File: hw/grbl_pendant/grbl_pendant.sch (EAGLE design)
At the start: 7 parts, among them IC1 ATMEGA644A, IC2 FT232RL, IC3 FT232RL, X1 PN61729-S, X2 PN61729-S

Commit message: sch/brd files updated
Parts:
- removed IC1: ATMEGA644A, atmel:ATMEGA644A
- removed IC3: FT232RL, ftdichip:FT232RL
- added C10: 100n, rcl:C-EUC0805
- added C2, C4: 20p, rcl:C-EUC0603K
- added C5, C6, C7: 100n, rcl:C-EUC0603K
- added C8, C9: 10u, rcl:C-EUC0805
- added CON1: MOLEX-53261-0671, SchlegelAr_Master:MOLEX-53261-0671
- added FERRIT1, FERRIT2, FERRIT3: (no value), rcl:R-EU_M0805
- added JP1: (no value), pinhead-2:PINHD-2X08_2.54
- added JP2: (no value), pinhead-2:PINHD-2X03_2.54
- added Q1: 14.7456 MHz, crystal:CRYSTALHC49UP
- added R1, R2, R3, R7: 220R, rcl:R-EU_R0603
- added R4, R5, R6: 100R, rcl:R-EU_R0603
- added U$1: MEGA162MA*A*, avr-7:MEGA162MA*A*
- added U$2: ARDUINONANO, rocketfarm:ARDUINONANO
- added X3: (no value), con-subd:F25HPS
- C1: value 100n -> 10u; device rcl:C-EUC0603 -> rcl:C-EUC0805
- X2: value PN61729-S -> (none); device con-berg:PN61729-S -> con-subd:F25HPS
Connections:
- removed net N$1: C1.2, IC3.3V3OUT, IC3.VCCIO
- removed net N$2: IC1.(PCINT24/RXD0)PD0
- removed net N$3: IC1.(PCINT25/TXD0)PD1
- removed net RXD_UC: IC3.RXD
- removed net TXD_UC: IC3.TXD
- removed net USBDM1: IC3.USBDM, X2.2
- removed net USBDP1: IC3.USBDP, X2.3
- new net !RESET: CON1.RESET
- new net BTN1: U$1.(AD0)PA0, X3-19.F
- new net BTN2: U$1.(AD1)PA1, X3-18.F
- new net BTN3: U$1.(AD2)PA2, X3-17.F
- new net BTN4: U$1.(AD3)PA3, X3-16.F
- new net BTN5: U$1.(AD4)PA4, X3-15.F
- new net BTN6: U$1.(AD5)PA5, X3-14.F
- new net BTN_JOG: U$1.(AD6)PA6, X3-13.F
- new net COOLING_ENABLE: U$2.A3, X2-17.F
- new net CYCLE_START/RESUME: U$2.A2, X2-18.F
- new net DISP_D0: U$1.(A8)PC0, X3-3.F
- new net DISP_D1: U$1.(A9)PC1, X3-4.F
- new net DISP_D2: U$1.(A10)PC2, X3-5.F
- new net DISP_D3: U$1.(A11)PC3, X3-6.F
- new net DISP_D4: U$1.(A12)PC4, X3-7.F
- new net DISP_D5: U$1.(A13)PC5, X3-8.F
- new net DISP_D6: U$1.(A14)PC6, X3-9.F
- new net DISP_D7: U$1.(A15)PC7, X3-10.F
- new net DISP_ENABLE: U$1.(ALE)PE1, X3-12.F
- new net DISP_RS: U$1.(OC1B)PE2, X3-11.F
- new net ENCODER_A: U$1.(INT0)PD2, X3-20.F
- new net ENCODER_B: U$1.(INT1)PD3, X3-21.F
- new net ENCODER_BTN: U$1.(INT2)PE0, X3-22.F
- new net FEED/HOLD: U$2.A1, X2-19.F
- new net LED_SHIFT_RCK: U$1.(TOSC2)PD5, X3-23.F, X3-24.F
- new net LED_SHIFT_SCK: U$1.(WR)PD6
- new net LED_SHIFT_SI: U$1.(TOSC1)PD4, X3-25.F
- new net LIMIT_INT_X: C9.2, FERRIT3.2, R1.2, R4.1
- new net LIMIT_INT_Y: C8.2, FERRIT2.2, R3.2, R5.1
- new net LIMIT_INT_Z: C1.2, FERRIT1.2, R2.2, R6.1
- new net LIMIT_X: FERRIT3.1, X2-25.F
- new net LIMIT_X_DEBOUNCED: R4.2, U$2.D9
- new net LIMIT_Y: FERRIT2.1, X2-24.F
- new net LIMIT_Y_DEBOUNCED: R5.2, U$2.D10
- new net LIMIT_Z: FERRIT1.1, X2-23.F
- new net LIMIT_Z_DEBOUNCED: R6.2, U$2.D11
- new net MISO: CON1.MISO, JP1.13, JP1.14, U$1.(MISO)PB6
- new net MOSI: CON1.MOSI, JP1.10, JP1.9, U$1.(MOSI)PB5
- new net N$7: C4.2, Q1.2, U$1.XTAL2
- new net N$8: C2.1, Q1.1, U$1.XTAL1
- new net RESET/ABORT: U$2.A0, X2-20.F
- new net RESET_AVR: U$1.RESET, U$2.RESET1, X2-21.F
- new net RXD_BRIDGE: U$1.(RXD1)PB2, U$2.D1/TX
- new net SCK: CON1.SCK, JP1.11, JP1.12, U$1.(SCK)PB7
- new net SD_IO_1: JP2.3, U$1.(AD7)PA7
- new net SD_IO_2: JP2.4, U$1.(T1)PB1
- new net SD_IO_3: JP2.5, U$1.(T0)PB0
- new net SD_IO_4: JP2.6, U$1.(RD)PD7
- new net SPINDLE_DIR: U$2.D13, X2-16.F
- new net SPINDLE_ENABLE: U$2.D12, X2-1.F
- new net SS: JP1.7, JP1.8, U$1.(SS)PB4
- new net STEPPER_DISABLE: U$2.D8, X2-15.F
- new net TXD_BRIDGE: U$1.(TXD1)PB3, U$2.D0/RX
- new net X_DIR: U$2.D5, X2-2.F
- new net X_STEP: U$2.D2, X2-3.F
- new net Y_DIR: U$2.D6, X2-4.F
- new net Y_STEP: U$2.D3, X2-5.F
- new net Z_DIR: U$2.D7, X2-6.F
- new net Z_PROBE: R7.2, U$2.A5, X2-22.F
- new net Z_STEP: U$2.D4, X2-7.F
- net +5V: now also C10.1, C5.1, C6.1, C7.1, CON1.VCC, JP1.5, JP1.6, JP2.1, R1.1, R2.1, R3.1, R7.1, U$1.VCC, U$1.VCC1, U$1.VCC2, U$2.+5V, X2-8.F, X2-9.F, X3-1.F; no longer IC3.!RESET, IC3.VCC, X2.1
- net GND: now also C10.2, C2.2, C4.1, C5.2, C6.2, C7.2, C8.1, C9.1, CON1.GND, CON1.GND@1, CON1.GND@2, JP1.1, JP1.15, JP1.16, JP1.2, JP2.2, U$1.GND, U$1.GND1, U$1.GND2, U$2.GND, U$2.GND1, X2-10.F, X2-11.F, X2-12.F, X2-13.F, X3-2.F; no longer IC3.GND, IC3.GND@1, IC3.GND@2, IC3.TEST, X2.4, X2.S1, X2.S2
- net RXD_PC: now also U$1.(TXD0)PD1
- net TXD_PC: now also U$1.(RXD0)PD0

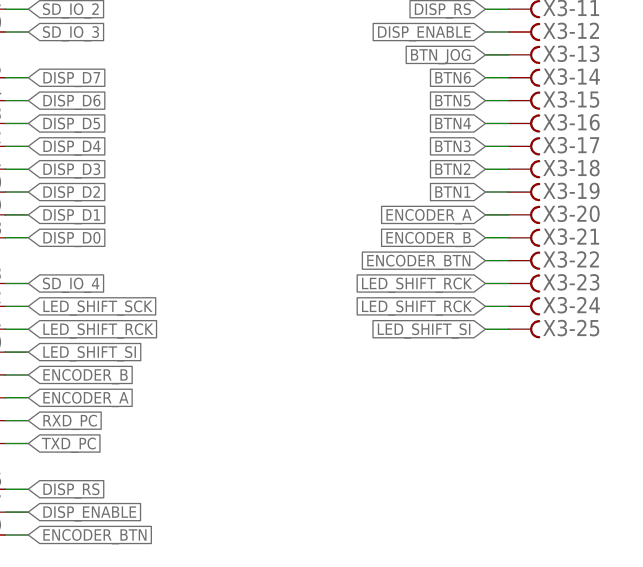
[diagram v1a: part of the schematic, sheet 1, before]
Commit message: grbl_pendant_peripheral v1 layout
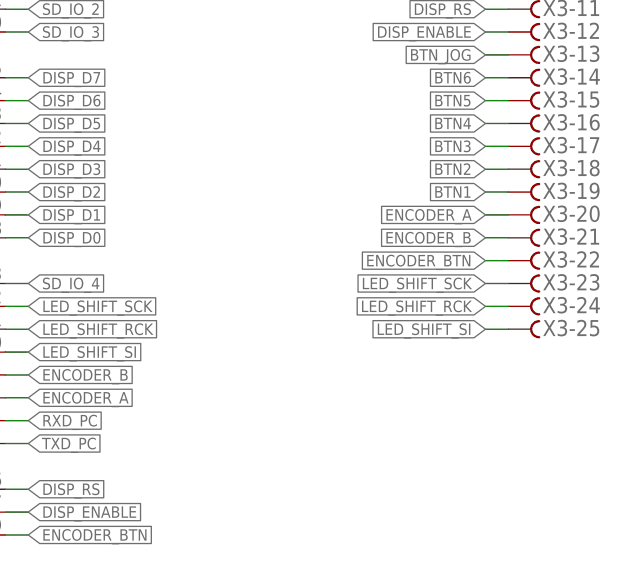
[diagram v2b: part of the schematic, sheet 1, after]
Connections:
- net LED_SHIFT_RCK: no longer X3-23.F
- net LED_SHIFT_SCK: now also X3-23.F
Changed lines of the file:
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@@
-</segment>
-<segment>
-<pinref part="X3" gate="-23" pin="F"/>
-<wire x1="241.3" y1="76.2" x2="238.76" y2="76.2" width="0.1524" layer="91"/>
-<label x="238.76" y="76.2" size="1.27" layer="95" rot="R180" xref="yes"/>
 </segment>
 <segment>
@@
 <pinref part="U$1" gate="G$1" pin="(WR)PD6"/>
 </segment>
+<segment>
+<pinref part="X3" gate="-23" pin="F"/>
+<wire x1="241.3" y1="76.2" x2="238.76" y2="76.2" width="0.1524" layer="91"/>
+<label x="238.76" y="76.2" size="1.27" layer="95" rot="R180" xref="yes"/>
+</segment>
 </net>

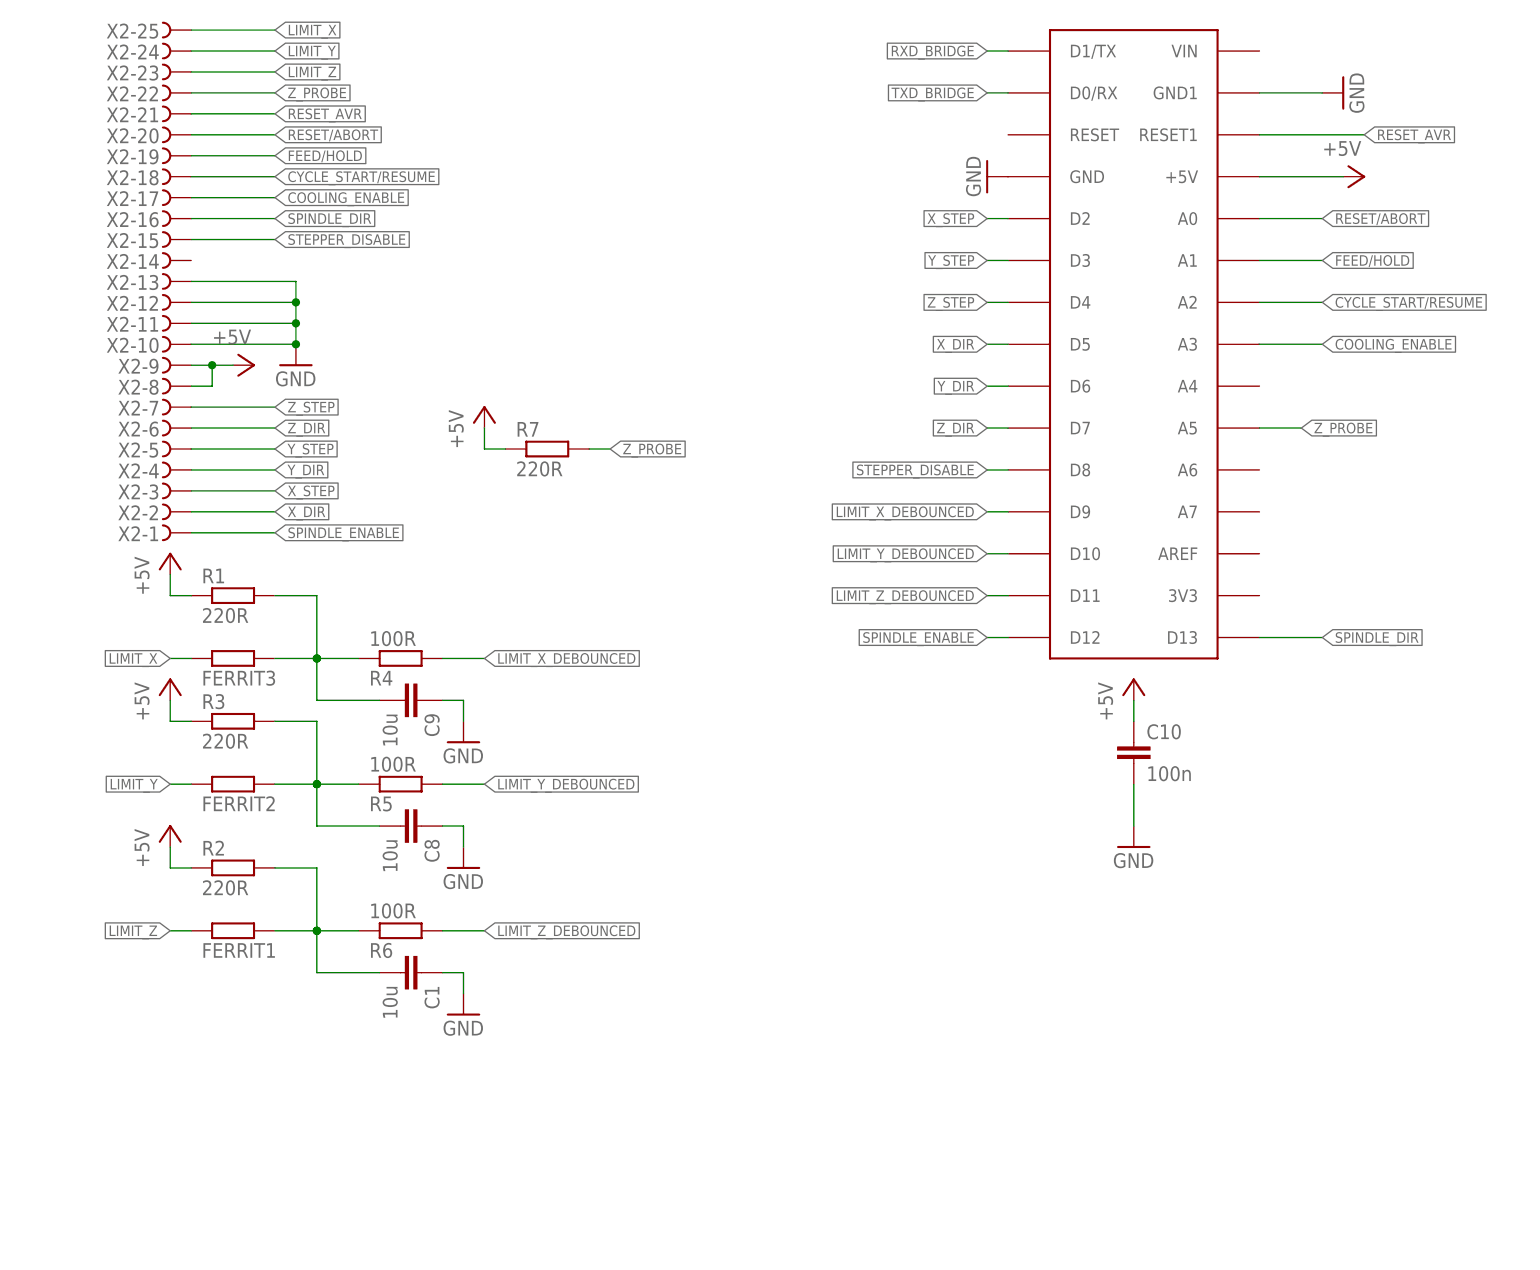
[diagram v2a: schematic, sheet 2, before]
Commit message: main board and pendant finished layouts
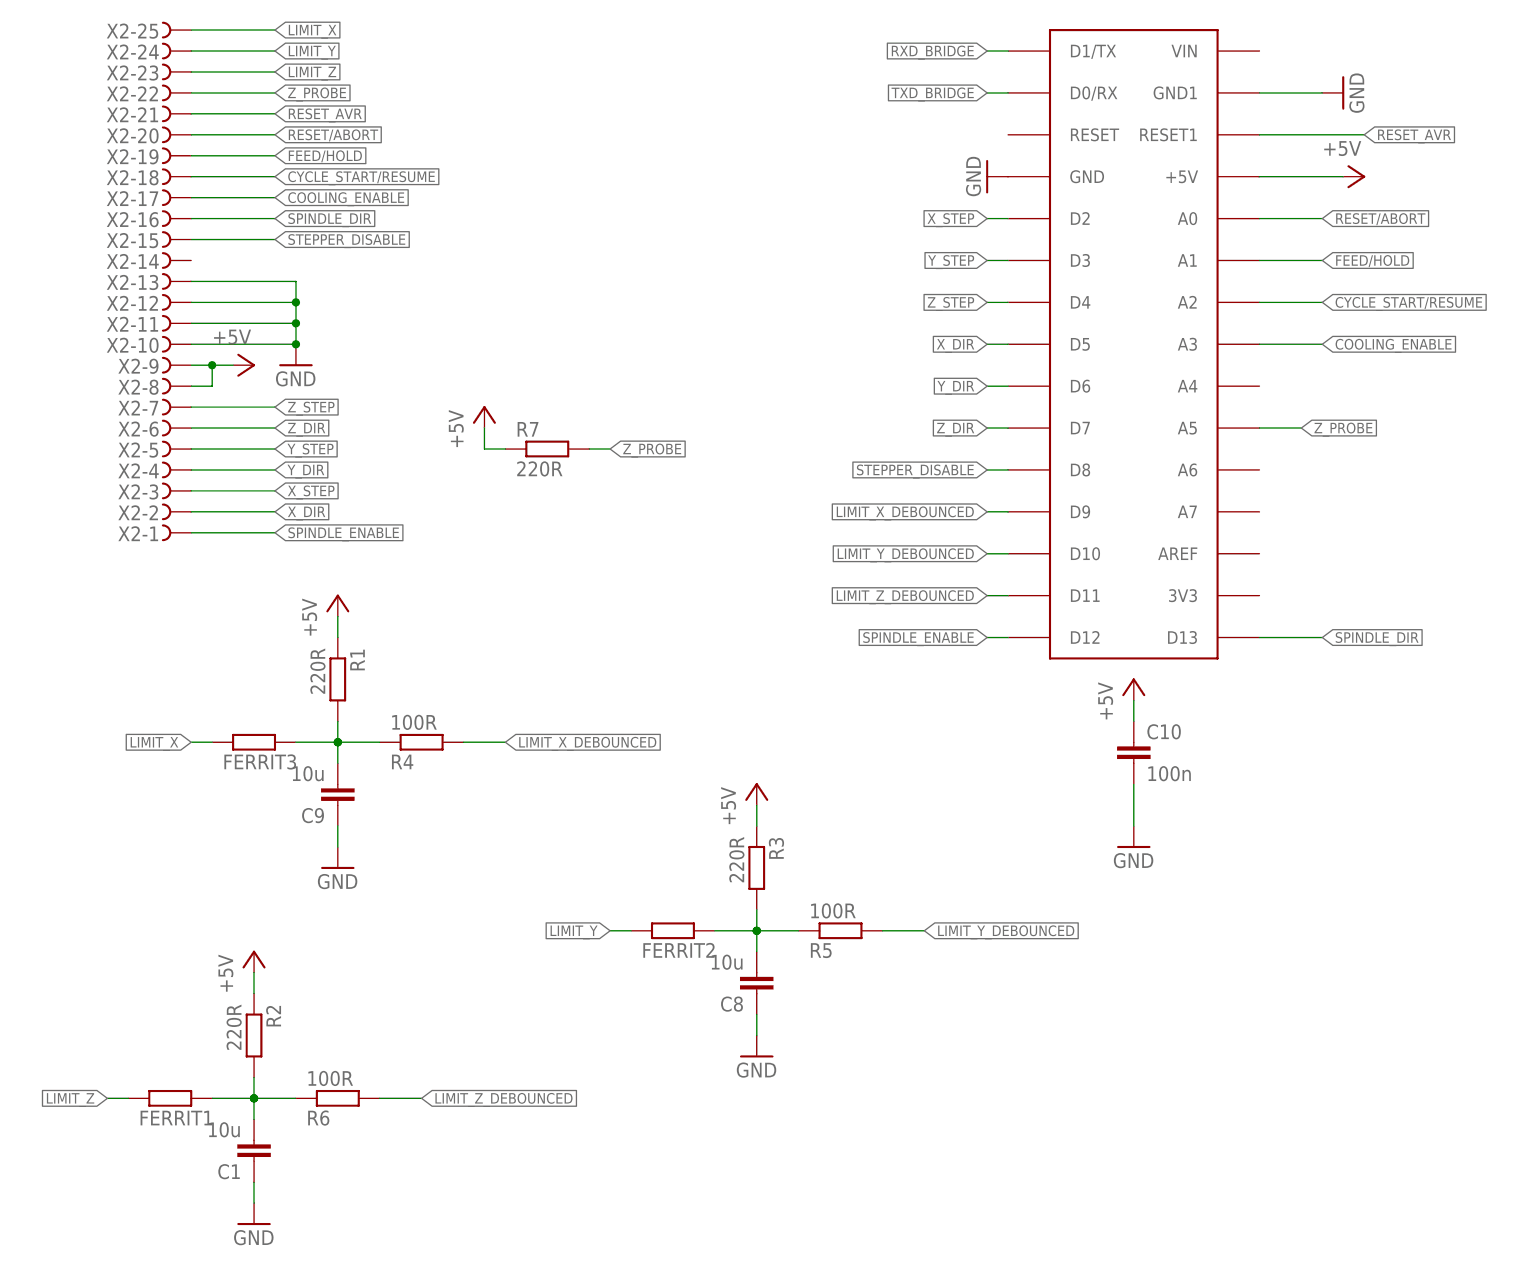
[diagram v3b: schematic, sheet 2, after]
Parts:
- renumbered U$1 to IC1
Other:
- moved on the sheet: C1, C8, C9, FERRIT1, FERRIT2, FERRIT3, R1, R2, R3, R4, R5, R6
